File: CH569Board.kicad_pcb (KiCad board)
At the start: 4 copper layers, 47.3 x 50.2 mm, 39 parts, among them CN1 BA42-80BT-1-NHB, J1 Conn_01x02_Male, J2 Conn_01x03_Male, U1 AMS1117-3.3, U2 CH569W, U3 AMS1117-1.2, U4 W25Q32JVSSIQ, X1 O705030MEEA4SC

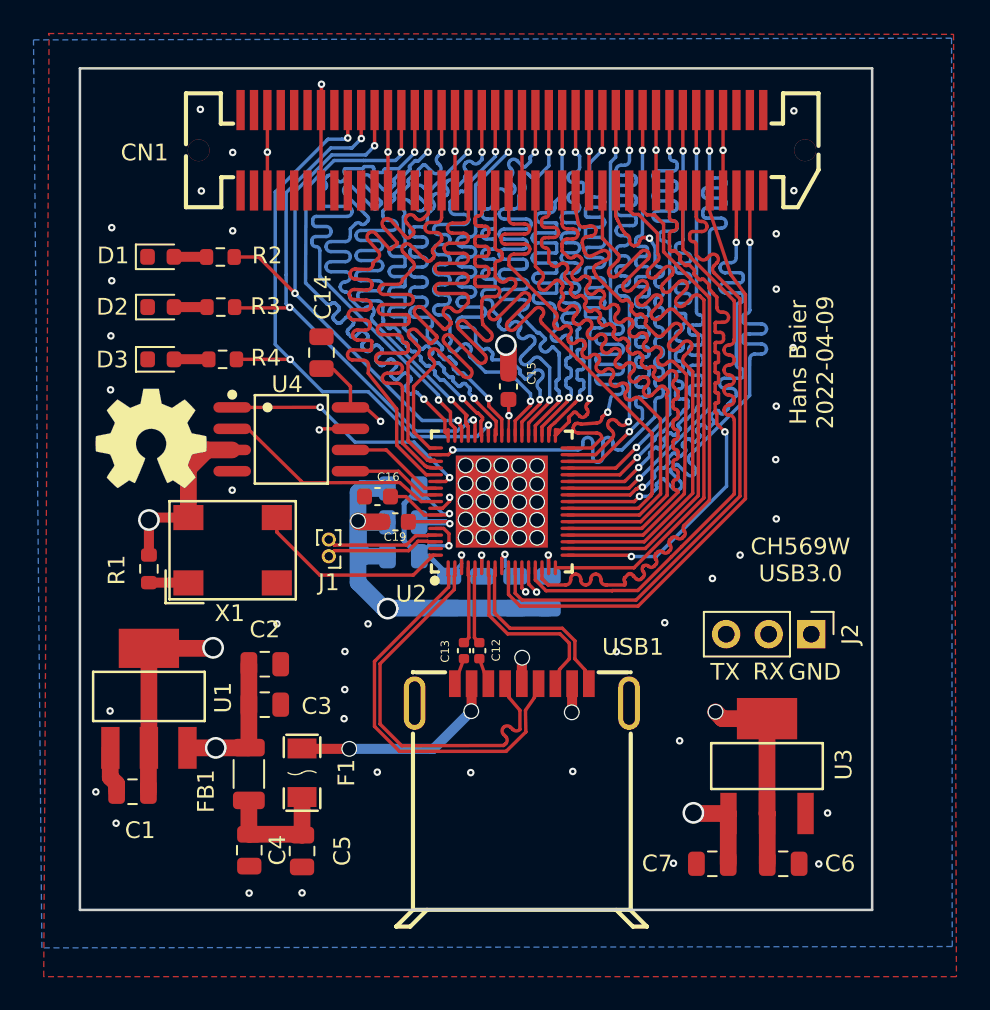
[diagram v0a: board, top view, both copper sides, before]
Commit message: New Edge cuts from FreeCAD and match the board to FPGA main board
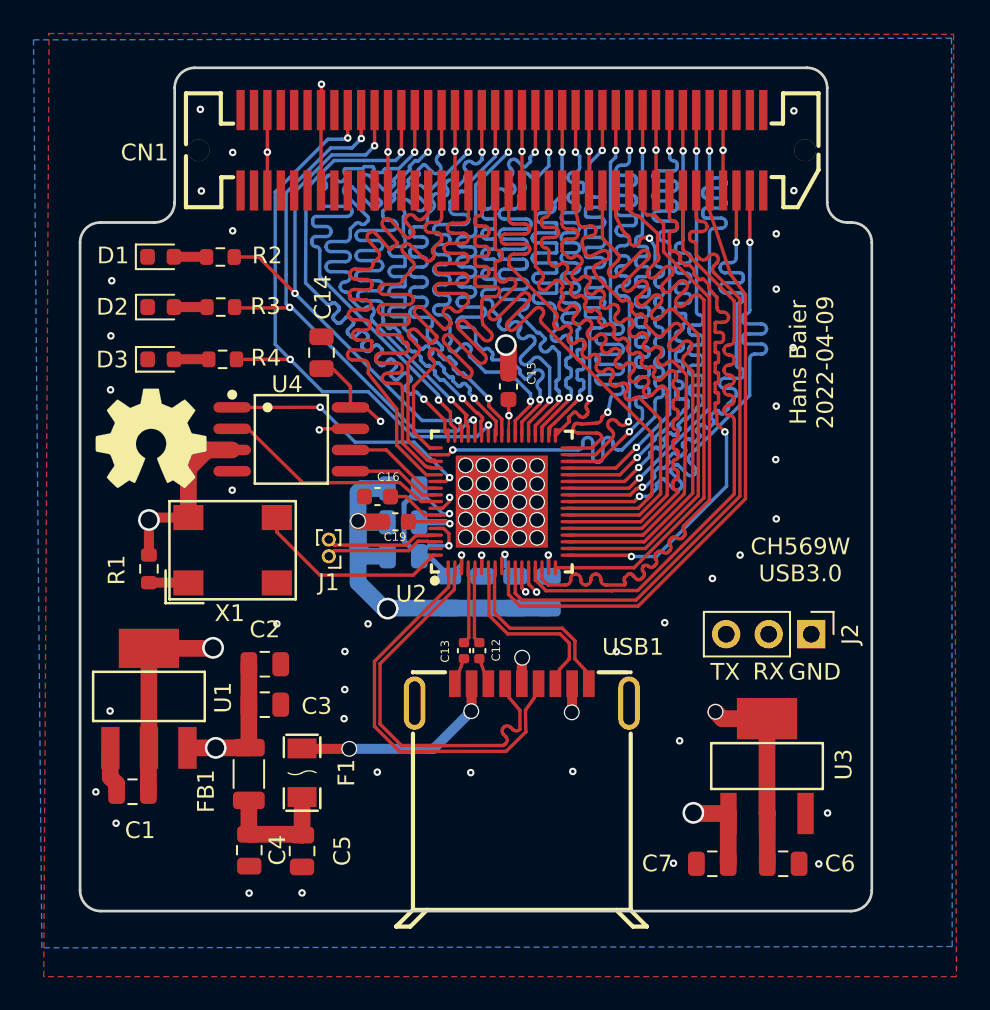
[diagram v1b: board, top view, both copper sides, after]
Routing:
- net GND: vias 76 -> 75
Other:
- board size 47.3 x 50.2 mm -> 47.3 x 50.3 mm
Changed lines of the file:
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@@
     )
   )
-  (gr_rect (start 100.42 127.735) (end 147.71 77.5) (layer "Edge.Cuts") (width 0.15) (fill none))
+  (gr_arc (start 147.688156 126.565943) (mid 147.325417 127.441673) (end 146.449687 127.804412) (layer "Edge.Cuts") (width 0.16))
+  (gr_arc (start 146.488156 86.701755) (mid 147.336684 87.053227) (end 147.688156 87.901755) (layer "Edge.Cuts") (width 0.16))
+  (gr_line (start 100.42878 87.901755) (end 100.42878 126.565943) (layer "Edge.Cuts") (width 0.16))
+  (gr_arc (start 106.072876 78.668286) (mid 106.424348 77.819758) (end 107.272876 77.468286) (layer "Edge.Cuts") (width 0.16))
+  (gr_arc (start 100.42878 87.901755) (mid 100.780252 87.053227) (end 101.62878 86.701755) (layer "Edge.Cuts") (width 0.16))
+  (gr_line (start 147.688156 126.565943) (end 147.688156 87.901755) (layer "Edge.Cuts") (width 0.16))
+  (gr_arc (start 106.072876 85.501755) (mid 105.721404 86.350283) (end 104.872876 86.701755) (layer "Edge.Cuts") (width 0.16))
+  (gr_line (start 145.028183 78.668286) (end 145.028183 85.501755) (layer "Edge.Cuts") (width 0.16))
+  (gr_arc (start 143.828183 77.468286) (mid 144.676711 77.819758) (end 145.028183 78.668286) (layer "Edge.Cuts") (width 0.16))
+  (gr_line (start 106.072876 85.501755) (end 106.072876 78.668286) (layer "Edge.Cuts") (width 0.16))
+  (gr_line (start 143.828183 77.468286) (end 107.272876 77.468286) (layer "Edge.Cuts") (width 0.16))
+  (gr_arc (start 146.228183 86.701755) (mid 145.379655 86.350283) (end 145.028183 85.501755) (layer "Edge.Cuts") (width 0.16))
+  (gr_arc (start 101.667249 127.804412) (mid 100.791519 127.441673) (end 100.42878 126.565943) (layer "Edge.Cuts") (width 0.16))
+  (gr_line (start 101.62878 86.701755) (end 104.872876 86.701755) (layer "Edge.Cuts") (width 0.16))
+  (gr_line (start 146.228183 86.701755) (end 146.488156 86.701755) (layer "Edge.Cuts") (width 0.16))
+  (gr_line (start 101.667249 127.804412) (end 146.449687 127.804412) (layer "Edge.Cuts") (width 0.16))
   (gr_text "Hans Baier\n2022-04-09" (at 144.11 95.05 90) (layer "F.SilkS")
     (effects (font (size 1 1) (thickness 0.15)))
@@
   (via (at 118.17 119.51) (size 0.45) (drill 0.2) (layers "F.Cu" "B.Cu") (free) (net 1))
   (via (at 116.24 112.31) (size 0.45) (drill 0.2) (layers "F.Cu" "B.Cu") (free) (net 1))
-  (via (at 102.32 87.01) (size 0.45) (drill 0.2) (layers "F.Cu" "B.Cu") (free) (net 1))
   (via (at 127.7112 104.4542) (size 0.95) (drill 0.8) (layers "F.Cu" "B.Cu") (net 1))
   (via (at 135.85 124.95) (size 0.45) (drill 0.2) (layers "F.Cu" "B.Cu") (free) (net 1))
@@
   (arc (start 131.212251 107.687749) (mid 131.424383 107.775617) (end 131.512251 107.987749) (width 0.20574) (layer "F.Cu") (net 80))
   (segment (start 136.492885 91.634018) (end 137.021319 91.105583) (width 0.20574) (layer "F.Cu") (net 81))
-  (segment (start 136.597055 90.257055) (end 136.597056 90.257056) (width 0.20574) (layer "F.Cu") (net 81))
   (segment (start 136.597056 90.68132) (end 136.068621 91.209754) (width 0.20574) (layer "F.Cu") (net 81))
-  (segment (start 135.748527 89.408527) (end 135.748528 89.408528) (width 0.20574) (layer "F.Cu") (net 81))
-  (segment (start 134.9 88.984264) (end 134.371565 89.512698) (width 0.20574) (layer "F.Cu") (net 81))
-  (segment (start 135.748527 89.832793) (end 135.748528 89.832792) (width 0.20574) (layer "F.Cu") (net 81))
-  (segment (start 133.493126 107.312) (end 128.803 107.312) (width 0.20574) (layer "F.Cu") (net 81))
-  (segment (start 137.445584 91.105584) (end 137.667749 91.327749) (width 0.20574) (layer "F.Cu") (net 81))
-  (segment (start 134.899999 88.984265) (end 134.9 88.984264) (width 0.20574) (layer "F.Cu") (net 81))
-  (segment (start 133.21 85.97) (end 133.459381 86.219381) (width 0.20574) (layer "F.Cu") (net 81))
   (segment (start 135.644358 90.785489) (end 135.644357 90.78549) (width 0.20574) (layer "F.Cu") (net 81))
+  (segment (start 137.445583 91.105583) (end 137.445584 91.105584) (width 0.20574) (layer "F.Cu") (net 81))
+  (segment (start 134.9 88.984264) (end 134.371565 89.512698) (width 0.20574) (layer "F.Cu") (net 81))
   (segment (start 134.9 87.35) (end 134.9 88.56) (width 0.20574) (layer "F.Cu") (net 81))
-  (segment (start 135.748528 89.832792) (end 135.220093 90.361226) (width 0.20574) (layer "F.Cu") (net 81))
   (segment (start 136.597055 90.681321) (end 136.597056 90.68132) (width 0.20574) (layer "F.Cu") (net 81))
-  (segment (start 136.492886 91.634017) (end 136.492885 91.634018) (width 0.20574) (layer "F.Cu") (net 81))
-  (segment (start 133.21 84.79) (end 133.21 85.97) (width 0.20574) (layer "F.Cu") (net 81))
+  (segment (start 134.79583 89.936961) (end 134.795829 89.936962) (width 0.20574) (layer "F.Cu") (net 81))
+  (segment (start 135.748528 89.832792) (end 135.220093 90.361226) (width 0.20574) (layer "F.Cu") (net 81))
+  (segment (start 134.899999 88.984265) (end 134.9 88.984264) (width 0.20574) (layer "F.Cu") (net 81))
+  (segment (start 136.597055 90.257055) (end 136.597056 90.257056) (width 0.20574) (layer "F.Cu") (net 81))
+  (segment (start 133.459381 86.219381) (end 133.7564 86.3092) (width 0.20574) (layer "F.Cu") (net 81))
+  (segment (start 137.445584 91.105584) (end 137.667749 91.327749) (width 0.20574) (layer "F.Cu") (net 81))
+  (segment (start 133.493126 107.312) (end 128.803 107.312) (width 0.20574) (layer "F.Cu") (net 81))
+  (segment (start 133.7564 86.3092) (end 134.9 87.35) (width 0.20574) (layer "F.Cu") (net 81))
   (segment (start 137.667749 91.327749) (end 137.667749 103.137377) (width 0.20574) (layer "F.Cu") (net 81))
-  (segment (start 133.459381 86.219381) (end 133.769381 86.219381) (width 0.20574) (layer "F.Cu") (net 81))
-  (segment (start 135.644357 90.78549) (end 136.172791 90.257055) (width 0.20574) (layer "F.Cu") (net 81))
+  (segment (start 135.748527 89.408527) (end 135.748528 89.408528) (width 0.20574) (layer "F.Cu") (net 81))
+  (segment (start 133.21 84.79) (end 133.21 85.97) (width 0.20574) (layer "F.Cu") (net 81))
+  (segment (start 133.21 85.97) (end 133.459381 86.219381) (width 0.20574) (layer "F.Cu") (net 81))
   (segment (start 137.667749 103.137377) (end 133.493126 107.312) (width 0.20574) (layer "F.Cu") (net 81))
-  (segment (start 137.445583 91.105583) (end 137.445584 91.105584) (width 0.20574) (layer "F.Cu") (net 81))
-  (segment (start 134.79583 89.936961) (end 134.795829 89.936962) (width 0.20574) (layer "F.Cu") (net 81))
+  (segment (start 135.748527 89.832793) (end 135.748528 89.832792) (width 0.20574) (layer "F.Cu") (net 81))
   (segment (start 134.795829 89.936962) (end 135.324263 89.408527) (width 0.20574) (layer "F.Cu") (net 81))
-  (segment (start 133.769381 86.219381) (end 134.9 87.35) (width 0.20574) (layer "F.Cu") (net 81))
-  (arc (start 136.172791 90.257055) (mid 136.384923 90.169187) (end 136.597055 90.257055) (width 0.20574) (layer "F.Cu") (net 81))
-  (arc (start 134.371565 89.512698) (mid 134.283697 89.72483) (end 134.371565 89.936962) (width 0.20574) (layer "F.Cu") (net 81))
-  (arc (start 135.220093 90.361226) (mid 135.132225 90.573358) (end 135.220093 90.78549) (width 0.20574) (layer "F.Cu") (net 81))
-  (arc (start 134.371565 89.936962) (mid 134.583698 90.02483) (end 134.79583 89.936961) (width 0.20574) (layer "F.Cu") (net 81))
+  (segment (start 135.644357 90.78549) (end 136.172791 90.257055) (width 0.20574) (layer "F.Cu") (net 81))
+  (segment (start 136.492886 91.634017) (end 136.492885 91.634018) (width 0.20574) (layer "F.Cu") (net 81))
+  (arc (start 135.324263 89.408527) (mid 135.536395 89.320659) (end 135.748527 89.408527) (width 0.20574) (layer "F.Cu") (net 81))
   (arc (start 136.068621 91.634018) (mid 136.280754 91.721886) (end 136.492886 91.634017) (width 0.20574) (layer "F.Cu") (net 81))
   (arc (start 136.597056 90.257056) (mid 136.684924 90.469189) (end 136.597055 90.681321) (width 0.20574) (layer "F.Cu") (net 81))
-  (arc (start 135.324263 89.408527) (mid 135.536395 89.320659) (end 135.748527 89.408527) (width 0.20574) (layer "F.Cu") (net 81))
   (arc (start 134.9 88.56) (mid 134.987868 88.772133) (end 134.899999 88.984265) (width 0.20574) (layer "F.Cu") (net 81))
+  (arc (start 135.220093 90.78549) (mid 135.432226 90.873358) (end 135.644358 90.785489) (width 0.20574) (layer "F.Cu") (net 81))
   (arc (start 136.068621 91.209754) (mid 135.980753 91.421886) (end 136.068621 91.634018) (width 0.20574) (layer "F.Cu") (net 81))
-  (arc (start 135.748528 89.408528) (mid 135.836396 89.620661) (end 135.748527 89.832793) (width 0.20574) (layer "F.Cu") (net 81))
   (arc (start 137.021319 91.105583) (mid 137.233451 91.017715) (end 137.445583 91.105583) (width 0.20574) (layer "F.Cu") (net 81))
-  (arc (start 135.220093 90.78549) (mid 135.432226 90.873358) (end 135.644358 90.785489) (width 0.20574) (layer "F.Cu") (net 81))
+  (arc (start 134.371565 89.512698) (mid 134.283697 89.72483) (end 134.371565 89.936962) (width 0.20574) (layer "F.Cu") (net 81))
+  (arc (start 136.172791 90.257055) (mid 136.384923 90.169187) (end 136.597055 90.257055) (width 0.20574) (layer "F.Cu") (net 81))
+  (arc (start 135.220093 90.361226) (mid 135.132225 90.573358) (end 135.220093 90.78549) (width 0.20574) (layer "F.Cu") (net 81))
+  (arc (start 134.371565 89.936962) (mid 134.583698 90.02483) (end 134.79583 89.936961) (width 0.20574) (layer "F.Cu") (net 81))
+  (arc (start 135.748528 89.408528) (mid 135.836396 89.620661) (end 135.748527 89.832793) (width 0.20574) (layer "F.Cu") (net 81))
   (segment (start 121.203 105.762) (end 121.16937 105.72837) (width 0.20574) (layer "F.Cu") (net 82))
   (segment (start 121.653 105.762) (end 121.203 105.762) (width 0.20574) (layer "F.Cu") (net 82))

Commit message: Big design fixup: Make Layer 3 a GND plane so signals reference ground. Eliminate one LED for better integrity of the signal traces, new board outline
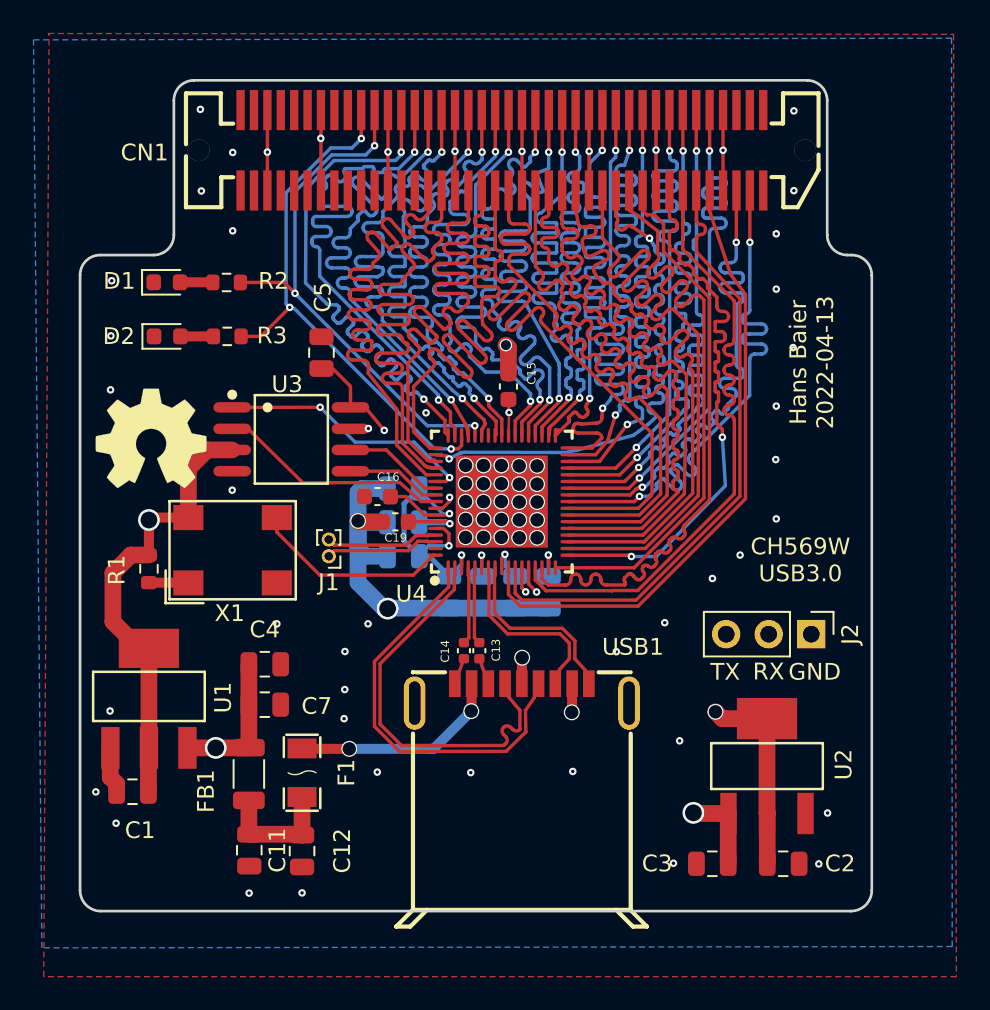
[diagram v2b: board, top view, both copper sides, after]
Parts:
- removed D3: red, LED_SMD:LED_0603_1608Metric
- removed R4: 1k, Resistor_SMD:R_0603_1608Metric
- moved D2 1.79 mm to (105.6, 93.5)
- moved R3 1.79 mm to (109.2, 93.5)
- moved R2 1.56 mm to (109.2, 90.3)
- moved D1 1.56 mm to (105.6, 90.3)
- renumbered C11 to C10, C4 to C11, C5 to C12, C12 to C13, C13 to C14, C6 to C2, C7 to C3, C2 to C4, C14 to C5, C8 to C6, C3 to C7, C9 to C8, C10 to C9, U3 to U2, U4 to U3, U2 to U4
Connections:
- CN1 pad 59: /LED2 -> /LED1
- CN1 pad 61: /LED1 -> /LED2
- CN1 pad 63: /LED0 -> unconnected-(CN1-Pad63)
- R2 pad 2: /LED2 -> /LED1
- R3 pad 2: /LED1 -> /LED2
- U4 pad 45: /LED0 -> unconnected-(U4-Pad45)
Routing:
- net /LED0: track 35.6 -> 0.00 mm, vias 3 -> 0
- net +3V3: track 64.5 -> 75.8 mm, vias 6 -> 5
- net /HD22: track 38.5 -> 34.2 mm
- net /HD28: track 38.2 -> 34.2 mm
- net /HD29: track 38.3 -> 34.6 mm
- net /HD2: track 36.8 -> 34.1 mm
- net +1V2: track 52.5 -> 55.1 mm
- net /HRACK: track 39.5 -> 37.5 mm
- net Net-(R4-Pad1): track 1.94 -> 0.00 mm
- net GND: track 73.9 -> 72.3 mm, vias 75 -> 76
- net /LED1: track 33.1 -> 32.2 mm
- net /VIO: track 35.8 -> 35.2 mm
- added copper zone on In2.Cu, net GND
- removed copper zone on In2.Cu, net +3V3
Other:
- board size 47.3 x 50.3 mm -> 47.3 x 49.6 mm
- board text added: "Hans Baier 2022-04-13"
- board text removed: "Hans Baier 2022-04-09"
